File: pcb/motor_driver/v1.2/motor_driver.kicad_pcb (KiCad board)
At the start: 4 copper layers, 50 x 50 mm, 93 parts, among them J1 XT60PW-M, J2 1-84953-1, J3 Conn_ARM_JTAG_SWD_10, J5 Conn, Q1 BSS138, Q2 HP8K22TB, Q3 HP8K22TB, Q4 HP8K22TB, SW1 RESET, SW2 USER, U1 USBLC6-4SC6, U10 STM32G431CB, U12 MCP2562-E-SN, U3 DRV8323S, U4 a1333, U8 ADP151AUJZ-3.3-R7, U9 NJM12877F33-TE1, Y1 XRCGB16M000FXN02R0

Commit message: perf: fix pcb for v1.2
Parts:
- removed the C22 at (123.7, 100.7)
- removed the C23 at (125.7, 116.1)
- removed the C28 at (133.1, 104.3)
- removed C29: 0.1u, Capacitor_SMD:C_0603_1608Metric
- removed the C5 at (103.6, 78.9)
- removed the D1 at (100.5, 120.2)
- removed the D2 at (103.4, 120.2)
- removed the D3 at (106.3, 120.2)
- removed the Q1 at (136.1, 115.0)
- removed the R1 at (100.5, 123.2)
- removed the R2 at (103.4, 123.2)
- removed the R20 at (136.1, 112.1)
- removed the R21 at (110.5, 116.9)
- removed the R3 at (106.3, 123.2)
- removed SP1: SMT-0440, omni:STM0440-T-R
- removed the U1 at (106.5, 78.6)
- added C6: 1u, Capacitor_SMD:C_0603_1608Metric_Pad1.08x0.95mm_HandSolder, F.Cu at (103.5, 112.0)
- C1, C2, C3, C4, C9: footprint Capacitor_SMD:C_0603_1608Metric -> Capacitor_SMD:C_0603_1608Metric_Pad1.08x0.95mm_HandSolder
- C13: renamed from C14; footprint Capacitor_SMD:C_0603_1608Metric -> Capacitor_SMD:C_0603_1608Metric_Pad1.08x0.95mm_HandSolder
- C14: renamed from C15; footprint Capacitor_SMD:C_0603_1608Metric -> Capacitor_SMD:C_0603_1608Metric_Pad1.08x0.95mm_HandSolder
- C15: renamed from C16; footprint Capacitor_SMD:C_0603_1608Metric -> Capacitor_SMD:C_0603_1608Metric_Pad1.08x0.95mm_HandSolder
- C16: renamed from C17; footprint Capacitor_SMD:C_0603_1608Metric -> Capacitor_SMD:C_0603_1608Metric_Pad1.08x0.95mm_HandSolder
- C17: renamed from C18; footprint Capacitor_SMD:C_0603_1608Metric -> Capacitor_SMD:C_0603_1608Metric_Pad1.08x0.95mm_HandSolder
- C18: renamed from C19; footprint Capacitor_SMD:C_0603_1608Metric -> Capacitor_SMD:C_0603_1608Metric_Pad1.08x0.95mm_HandSolder
- C21: renamed from C25; footprint Capacitor_SMD:C_0603_1608Metric -> Capacitor_SMD:C_0603_1608Metric_Pad1.08x0.95mm_HandSolder
- C24: value 2.2u -> 0.1u
- C26: renamed from C33; footprint Capacitor_SMD:C_0603_1608Metric -> Capacitor_SMD:C_0603_1608Metric_Pad1.08x0.95mm_HandSolder
- C5: renamed from C7; footprint Capacitor_SMD:C_0402_1005Metric -> Capacitor_SMD:C_0603_1608Metric_Pad1.08x0.95mm_HandSolder
- D1: renamed from D4; footprint LED_SMD:LED_0402_1005Metric -> LED_SMD:LED_0603_1608Metric
- D2: renamed from D5; footprint LED_SMD:LED_0402_1005Metric -> LED_SMD:LED_0603_1608Metric
- D3: renamed from D6; footprint LED_SMD:LED_0402_1005Metric -> LED_SMD:LED_0603_1608Metric
- D4: renamed from D7; footprint LED_SMD:LED_0402_1005Metric -> LED_SMD:LED_0603_1608Metric
- D5: renamed from D8; footprint LED_SMD:LED_0402_1005Metric -> LED_SMD:LED_0603_1608Metric
- D6: renamed from D9; footprint LED_SMD:LED_0402_1005Metric -> LED_SMD:LED_0603_1608Metric
- D7: renamed from D10; footprint LED_SMD:LED_0402_1005Metric -> LED_SMD:LED_0603_1608Metric
- J1: value XT60PW-M -> XT30
- R17: renamed from R22; footprint Resistor_SMD:R_0603_1608Metric -> Resistor_SMD:R_0603_1608Metric_Pad0.98x0.95mm_HandSolder
- R18: renamed from R24; footprint Resistor_SMD:R_0603_1608Metric -> Resistor_SMD:R_0603_1608Metric_Pad0.98x0.95mm_HandSolder
- R19: renamed from R23; footprint Resistor_SMD:R_0603_1608Metric -> Resistor_SMD:R_0603_1608Metric_Pad0.98x0.95mm_HandSolder
- R20: renamed from R25; footprint Resistor_SMD:R_0603_1608Metric -> Resistor_SMD:R_0603_1608Metric_Pad0.98x0.95mm_HandSolder
- SW1, SW2: footprint bldc_lib:SKRPACE010 -> half_mouse_lib:TVAF06-A020B-R
- moved C21 1.86 mm to (109.5, 116.5), turned to 90 degrees
- moved C24 1.55 mm to (131.7, 112.5)
- moved R18 0.81 mm to (115.4, 116.5)
- moved D7 0.70 mm to (133.6, 88.3)
- moved D6 0.68 mm to (135.4, 88.3)
- moved D2 0.60 mm to (118.8, 122.8)
- moved R11 0.60 mm to (118.8, 119.8)
- moved D3 0.59 mm to (121.6, 122.8)
- moved R13 0.59 mm to (121.6, 119.8)
- moved R10 0.57 mm to (130.1, 119.8)
- moved D1 0.57 mm to (130.1, 122.9)
- moved D4 0.56 mm to (124.4, 122.8)
- moved R14 0.56 mm to (124.4, 119.8)
- moved D5 0.55 mm to (127.2, 122.8)
- moved R15 0.55 mm to (127.2, 119.8)
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- renumbered C11 to C10, C12 to C11, C13 to C12, C20 to C19, C21 to C20, C26 to C22, C27 to C23, C30 to C25, C34 to C27, C36 to C28, C10 to C7, J2 to J3, J3 to J4, Q2 to Q1, Q3 to Q2, Q4 to Q3, R4 to R1, R13 to R10, R14 to R11, R15 to R12, R16 to R13, R17 to R14, R18 to R15, R19 to R16, R5 to R2, R26 to R21, R27 to R22, R28 to R23, R6 to R3, R7 to R4, R8 to R5, R9 to R6, R10 to R7, R11 to R8, R12 to R9, U3 to U1, U4 to U2, U8 to U3, U9 to U4, U10 to U5, U12 to U6
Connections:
- net /drv8323/INHA renamed /stm32g431cb/TIM4_INHA
- net /drv8323/INHB renamed /stm32g431cb/TIM4_INHB
- net /drv8323/INHC renamed /stm32g431cb/TIM4_INHC
- C24 pad 1: Net-(C24-Pad1) -> +3.3V
- C26 pad 1: +3.3V -> /stm32g431cb/SW1
- R18 pad 2: Net-(R24-Pad2) -> /stm32g431cb/SW1
- SW1 pad 1: Net-(R21-Pad2) -> /stm32g431cb/NRST
- SW1 pad 2: unconnected-(SW1-Pad2) -> GND
- SW2 pad 1: Net-(R24-Pad2) -> GND
- U1 pad 33: +3.3V -> Net-(U1-DVDD)
- U5 pad 19: Net-(C23-Pad1) -> GND
- U5 pad 23: Net-(C24-Pad1) -> GND
- U5 pad 35: Net-(C28-Pad1) -> GND
- U5 pad 47: Net-(C22-Pad1) -> GND
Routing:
- net /stm32g431cb/TIM4_INHA: track 52.7 -> 40.1 mm
- net /stm32g431cb/TIM4_INHB: track 47.0 -> 37.0 mm
- net Net-(Q1-Pad3): track 8.27 -> 0.00 mm
- net /stm32g431cb/TIM15_SP: track 8.17 -> 0.00 mm, vias 1 -> 0
- net /stm32g431cb/TIM4_INHC: track 42.5 -> 34.8 mm
- net /drv8323/HALL_W: track 48.2 -> 40.7 mm
- net /drv8323/HALL_U: track 47.8 -> 40.7 mm, vias 3 -> 2
- net GND: track 871.3 -> 864.7 mm, vias 105 -> 107
- net +3.3V: track 44.9 -> 39.2 mm, vias 8 -> 7
- net /drv8323/HALL_V: track 45.1 -> 40.5 mm
- net Net-(C23-Pad1): track 3.90 -> 0.00 mm
- net Net-(C24-Pad1): track 3.19 -> 0.00 mm
- net +5V: track 35.4 -> 32.4 mm, vias 6 -> 5
- net Net-(U1-DVDD): track 0.00 -> 2.56 mm
- net Net-(C22-Pad1): track 2.50 -> 0.00 mm
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
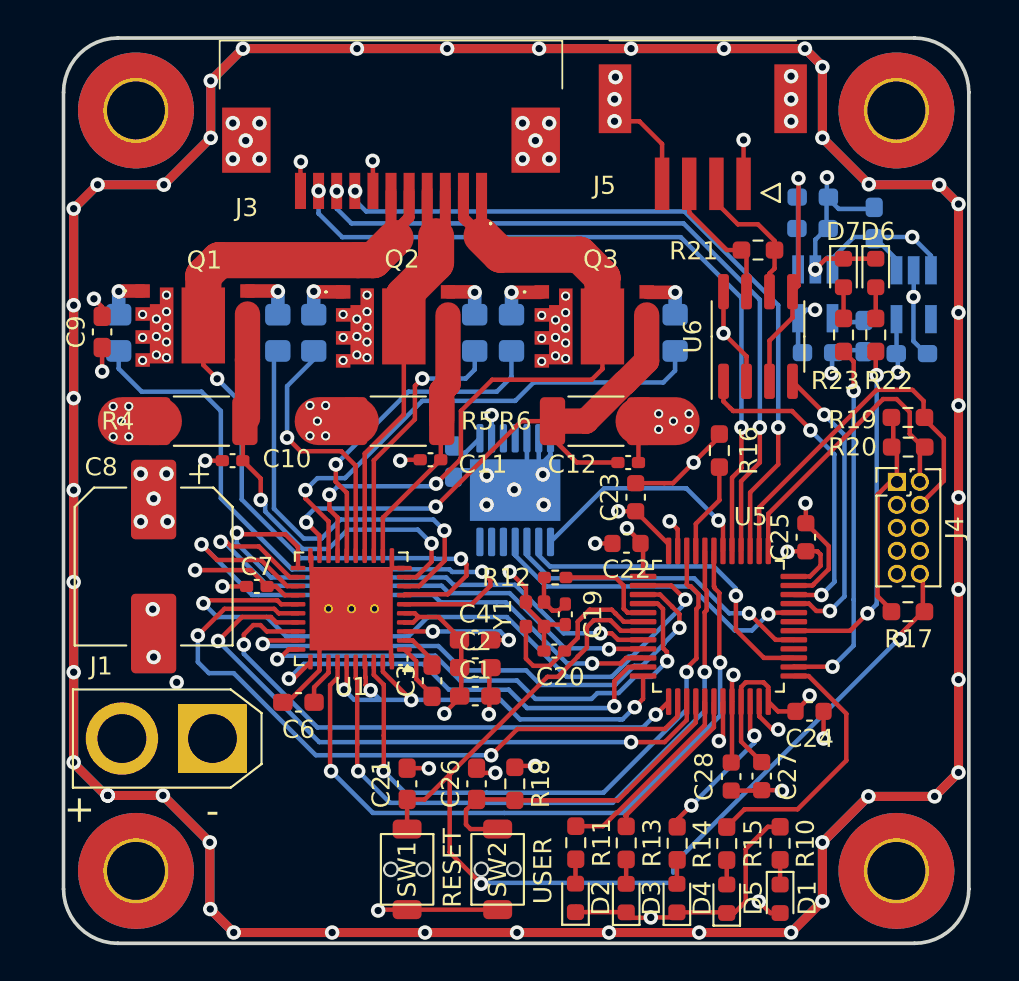
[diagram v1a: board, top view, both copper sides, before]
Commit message: perf: update motor driver pdb
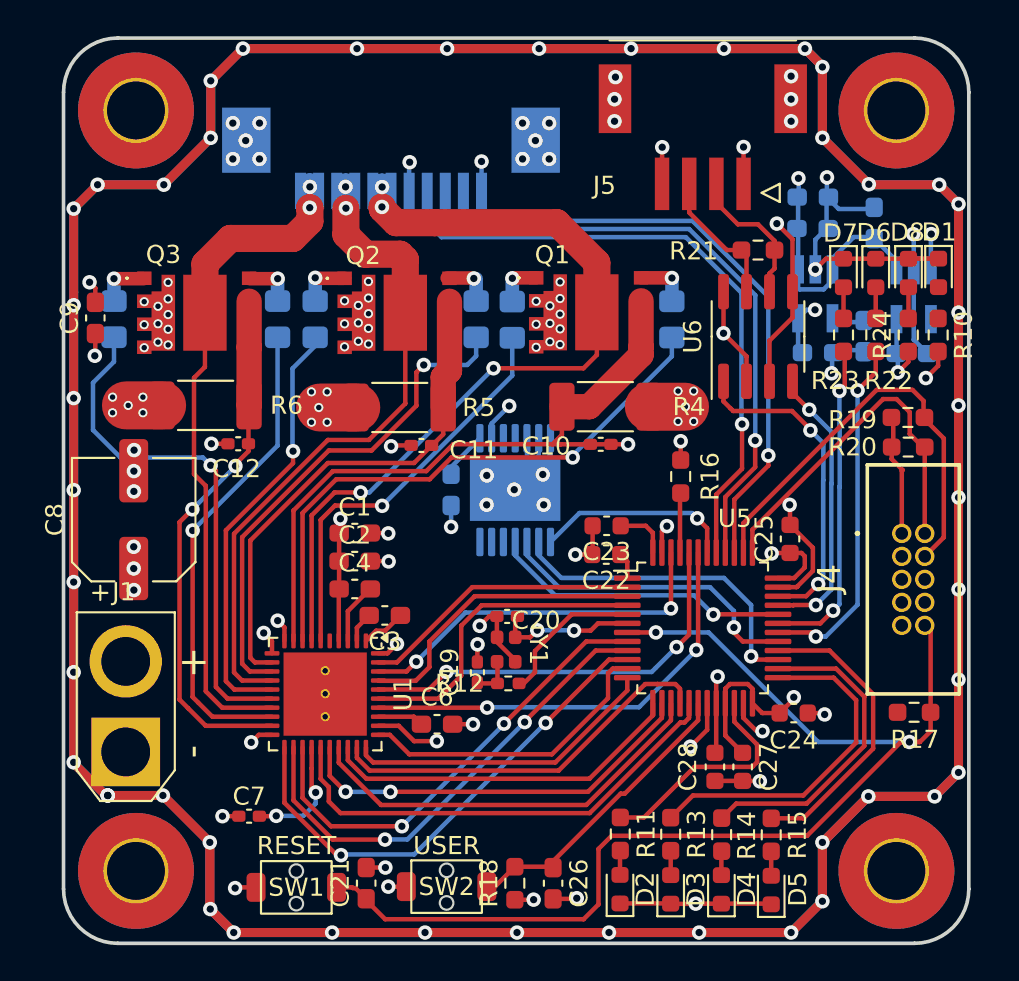
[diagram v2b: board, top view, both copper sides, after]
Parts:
- added D8: LED, LED_SMD:LED_0603_1608Metric, F.Cu at (137.2, 88.3)
- added R24: 1k, Resistor_SMD:R_0603_1608Metric_Pad0.98x0.95mm_HandSolder, F.Cu at (137.2, 91.7)
- C8: footprint Capacitor_SMD:CP_Elec_8x10.5 -> Capacitor_SMD:CP_Elec_6.3x3.9
- J3: moved to B.Cu
- J4: footprint Connector_PinHeader_1.27mm:PinHeader_2x05_P1.27mm_Vertical -> mylib:322110010000
- moved D1 35.7 mm to (138.8, 88.3)
- moved R10 29.4 mm to (138.8, 91.7)
- moved R4 22.3 mm to (120.5, 95.7), turned to 180 degrees
- moved Q3 22.0 mm to (97.9, 90.5)
- moved R3 22.0 mm to (93.3, 90.8)
- moved R9 22.0 mm to (102.3, 90.8)
- moved R7 21.8 mm to (124.1, 90.9)
- moved Q1 21.7 mm to (119.5, 90.5)
- moved R1 21.7 mm to (115.3, 90.9)
- moved R6 21.6 mm to (98.4, 95.6), turned to 0 degrees
- moved C12 21.6 mm to (100.2, 97.7), turned to 180 degrees
- moved C10 20.4 mm to (120.2, 97.8), turned to 0 degrees
- moved C7 12.7 mm to (100.8, 118.3)
- moved C1 11.2 mm to (106.6, 102.7)
- moved C2 8.89 mm to (106.6, 104.2)
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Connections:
- D1 pad 1: Net-(D1-K) -> GND
- D1 pad 2: +3.3V -> Net-(D1-A)
- R10 pad 1: Net-(D1-K) -> +3.3V
- R10 pad 2: GND -> Net-(D1-A)
- U1 pad 21: /stm32g431cb/ADC1_1 -> /stm32g431cb/ADC1_3
- U1 pad 23: /stm32g431cb/ADC1_3 -> /stm32g431cb/ADC1_1
- U1 pad 35: /stm32g431cb/INLX -> /stm32g431cb/INLA
- U1 pad 37: /stm32g431cb/INLX -> /stm32g431cb/INLB
- U1 pad 39: /stm32g431cb/INLX -> /stm32g431cb/INLC
- U5 pad 12: /stm32g431cb/INLX -> /stm32g431cb/DRV_ENABLE
- U5 pad 16: /stm32g431cb/SW1 -> /stm32g431cb/SS_DRV
- U5 pad 17: /stm32g431cb/LED1 -> /stm32g431cb/FAULTB
- U5 pad 18: /stm32g431cb/LED2 -> /stm32g431cb/SW1
- U5 pad 2: /stm32g431cb/FAULTB -> /stm32g431cb/INLC
- U5 pad 22: /stm32g431cb/LED3 -> /stm32g431cb/LED1
- U5 pad 25: /stm32g431cb/LED4 -> /stm32g431cb/LED2
- U5 pad 26: /stm32g431cb/LED_CAN_RX -> /stm32g431cb/LED3
- U5 pad 28: /stm32g431cb/TIM15_SP -> /stm32g431cb/LED4
- U5 pad 3: /stm32g431cb/SS_DRV -> /stm32g431cb/INLB
- U5 pad 31: unconnected-(U5-PA9-Pad31) -> /stm32g431cb/LED_CAN_RX
- U5 pad 39: /drv8323/HALL_V -> /drv8323/HALL_W
- U5 pad 4: /stm32g431cb/DRV_ENABLE -> /stm32g431cb/INLA
- U5 pad 41: /drv8323/HALL_W -> /drv8323/HALL_V
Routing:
- net GND: track 864.7 -> 837.6 mm, vias 107 -> 120
- net /stm32g431cb/INLX: track 25.7 -> 0.00 mm, vias 4 -> 0
- net /stm32g431cb/INLA: track 0.00 -> 17.5 mm
- net /stm32g431cb/INLB: track 0.00 -> 16.5 mm
- net /stm32g431cb/TIM4_INHA: track 40.1 -> 24.3 mm
- net /stm32g431cb/INLC: track 0.00 -> 15.5 mm
- net /drv8323/SPI1_MISO: track 38.0 -> 22.8 mm
- net /stm32g431cb/TIM4_INHC: track 34.8 -> 20.7 mm
- net /stm32g431cb/TIM4_INHB: track 37.0 -> 22.9 mm
- net /drv8323/SLB: track 14.8 -> 28.4 mm
- net /drv8323/SLA: track 26.0 -> 39.2 mm, vias 2 -> 0
- net /stm32g431cb/FAULTB: track 39.3 -> 26.3 mm, vias 2 -> 0
- net /drv8323/GLB: track 15.0 -> 28.0 mm
- net /drv8323/SHB: track 24.7 -> 36.8 mm, vias 0 -> 2
- net /drv8323/GHA: track 34.7 -> 22.7 mm
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
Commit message: wip: can settings
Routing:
- net +3.3V: track 31.1 -> 32.0 mm, vias 5 -> 7
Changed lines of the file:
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@@
-	)
-	(segment
-		(start 121.66 104.225)
-		(end 121.275 103.84)
-		(width 0.25)
-		(layer "F.Cu")
-		(net 8)
 	)
 	(segment
@@
 	)
 	(segment
+		(start 121.315 102.27)
+		(end 121.295 102.25)
+		(width 0.25)
+		(layer "F.Cu")
+		(net 8)
+	)
+	(segment
 		(start 136.3504 96.2814)
 		(end 136.335 96.266)
@@
 	)
 	(segment
+		(start 123.0725 102.8425)
+		(end 122.5 102.27)
+		(width 0.25)
+		(layer "F.Cu")
+		(net 8)
+	)
+	(segment
+		(start 122.03 103.84)
+		(end 121.275 103.84)
+		(width 0.25)
+		(layer "F.Cu")
+		(net 8)
+	)
+	(segment
 		(start 136.82 99.22)
 		(end 136.82 102.67)
@@
 	)
 	(segment
-		(start 121.66 105.14)
-		(end 121.66 104.225)
+		(start 122.3 104.28)
+		(end 122.3 104.09)
 		(width 0.25)
 		(layer "F.Cu")
@@
 	)
 	(segment
-		(start 122.68 102.25)
-		(end 121.295 102.25)
+		(start 122.04 103.83)
+		(end 122.03 103.84)
 		(width 0.25)
 		(layer "F.Cu")
@@
 	)
 	(segment
-		(start 123.0725 102.6425)
-		(end 122.68 102.25)
-		(width 0.25)
-		(layer "F.Cu")
-		(net 8)
-	)
-	(segment
 		(start 128.5725 111.249315)
 		(end 128.311985 110.9888)
@@
 	)
 	(segment
+		(start 121.66 104.92)
+		(end 122.3 104.28)
+		(width 0.25)
+		(layer "F.Cu")
+		(net 8)
+	)
+	(segment
+		(start 122.3 104.09)
+		(end 122.04 103.83)
+		(width 0.25)
+		(layer "F.Cu")
+		(net 8)
+	)
+	(segment
 		(start 129.6573 103.7504)
 		(end 129.6325 103.7752)
@@
 	)
 	(segment
-		(start 123.0725 103.7275)
-		(end 123.0725 102.6425)
-		(width 0.25)
-		(layer "F.Cu")
-		(net 8)
-	)
-	(segment
 		(start 129.1124 112.5924)
 		(end 130.0773 112.5924)
@@
 	)
 	(segment
+		(start 121.66 105.14)
+		(end 121.66 104.92)
+		(width 0.25)
+		(layer "F.Cu")
+		(net 8)
+	)
+	(segment
 		(start 136.87 99.17)
 		(end 136.82 99.22)
@@
 	)
 	(segment
+		(start 122.5 102.27)
+		(end 121.315 102.27)
+		(width 0.25)
+		(layer "F.Cu")
+		(net 8)
+	)
+	(segment
 		(start 131.4613 103.9276)
 		(end 131.2841 103.7504)
@@
 	)
 	(segment
+		(start 123.0725 103.7275)
+		(end 123.0725 102.8425)
+		(width 0.25)
+		(layer "F.Cu")
+		(net 8)
+	)
+	(segment
 		(start 116.480391 122.905)
 		(end 116.4875 122.897891)
@@
 	)
 	(via
+		(at 122.5 102.27)
+		(size 0.8)
+		(drill 0.4)
+		(layers "F.Cu" "B.Cu")
+		(net 8)
+	)
+	(via
 		(at 116.4875 122.897891)
 		(size 0.8)
@@
 		(size 0.8)
 		(drill 0.4)
+		(layers "F.Cu" "B.Cu")
+		(net 8)
+	)
+	(via
+		(at 122.3 104.28)
+		(size 0.8)
+		(drill 0.4)

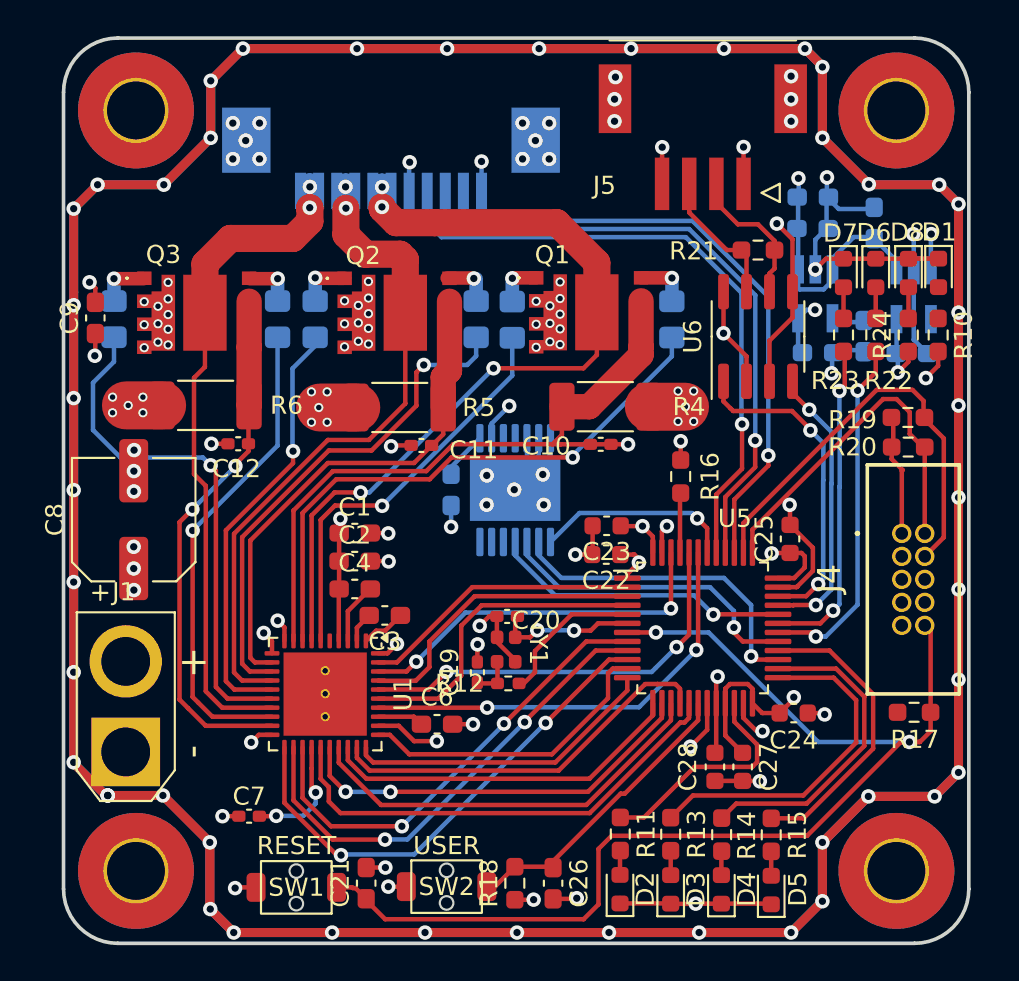
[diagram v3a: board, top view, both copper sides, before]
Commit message: feat: add additional CAN connetctor
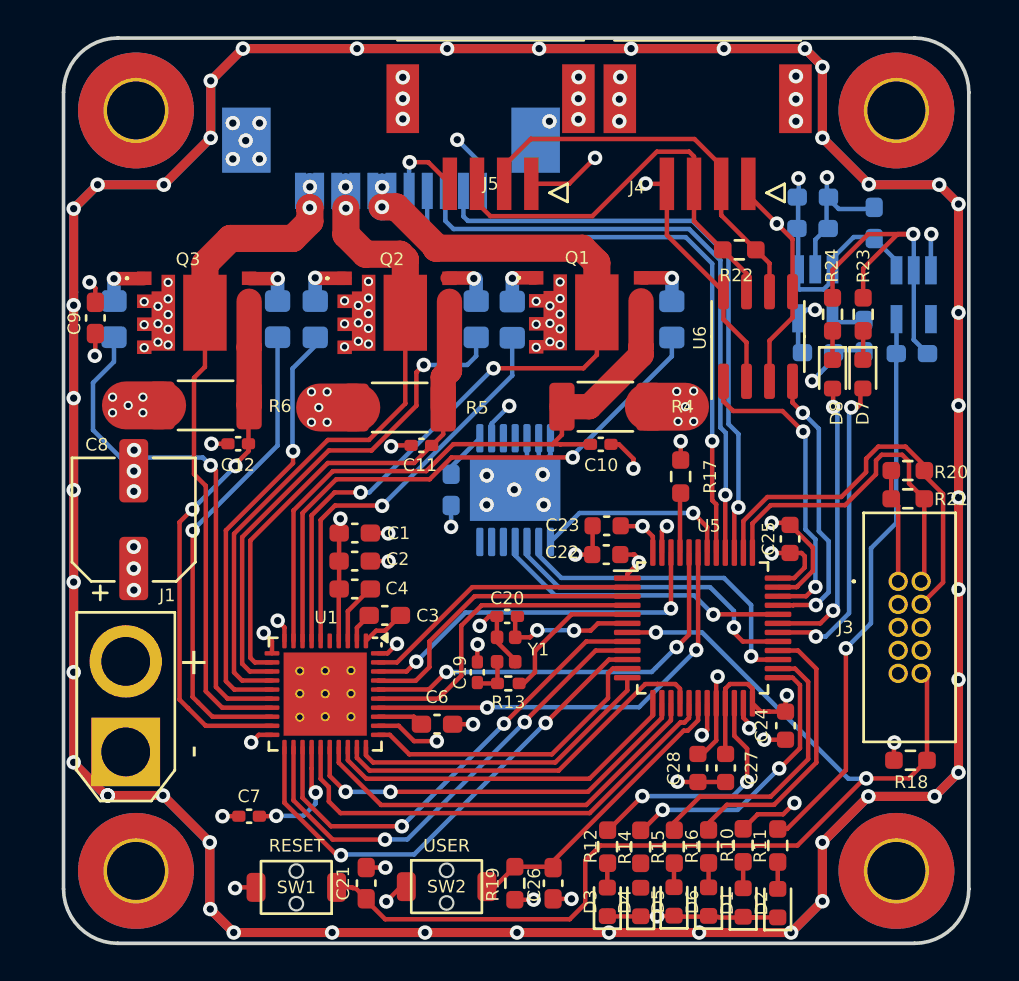
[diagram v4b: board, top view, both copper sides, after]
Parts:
- removed the D8 at (137.2, 88.3)
- removed the R24 at (137.2, 91.7)
- added D2: LED, LED_SMD:LED_0603_1608Metric, F.Cu at (130.0, 123.1)
- added J5: Conn, mylib:21322604YY, F.Cu at (114.1, 83.4)
- added R11: 1k, Resistor_SMD:R_0603_1608Metric_Pad0.98x0.95mm_HandSolder, F.Cu at (130.0, 119.9)
- J4: renamed from J5; footprint bldc_lib:21322604YY -> mylib:21322604YY
- moved D1 36.4 mm to (128.1, 123.1), turned to 90 degrees
- moved R10 30.2 mm to (128.1, 119.9), turned to -90 degrees
- moved D7 5.64 mm to (134.7, 93.9)
- moved D8 5.63 mm to (133.0, 93.9)
- moved D6 3.52 mm to (126.2, 123.0)
- moved R16 3.52 mm to (126.2, 120.0)
- moved R20 2.93 mm to (137.2, 99.2)
- moved R21 2.86 mm to (137.2, 100.8)
- moved D5 2.70 mm to (124.2, 123.0)
- moved R15 2.70 mm to (124.3, 120.0)
- moved R18 2.66 mm to (137.3, 115.2)
- moved J3 2.66 mm to (136.6, 105.3)
- moved D4 1.80 mm to (122.4, 123.0)
- moved R14 1.80 mm to (122.4, 120.0)
- moved R23 1.33 mm to (134.7, 90.6)
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- renumbered D2 to D3, D3 to D4, D4 to D5, D5 to D6, D6 to D7, D7 to D8, J3 to J2, J4 to J3, R11 to R12, R12 to R13, R13 to R14, R14 to R15, R15 to R16, R16 to R17, R17 to R18, R18 to R19, R19 to R20, R20 to R21, R21 to R22, R22 to R23, R23 to R24
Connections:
- D7 pad 1: GND -> Net-(D7-K)
- D7 pad 2: Net-(D6-A) (its old number) -> /stm32g431cb/LED_CAN_TX
- D8 pad 1: GND -> Net-(D8-K)
- D8 pad 2: Net-(D7-A) -> /stm32g431cb/LED_CAN_RX
- R23 pad 1: /stm32g431cb/LED_CAN_TX -> Net-(D7-K)
- R23 pad 2: Net-(D6-A) (its old number) -> GND
- R24 pad 1: /stm32g431cb/LED_CAN_RX -> Net-(D8-K)
- R24 pad 2: Net-(D7-A) -> GND
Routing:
- net GND: track 837.6 -> 854.7 mm
- net /stm32g431cb/CAN_H: track 7.75 -> 23.6 mm
- net /stm32g431cb/CAN_L: track 8.05 -> 22.3 mm
- net +3.3VA: track 64.2 -> 75.3 mm
- net +5V: track 33.2 -> 39.8 mm
- net /stm32g431cb/NRST: track 64.6 -> 60.1 mm
- net /stm32g431cb/LED2: track 19.1 -> 15.4 mm, vias 0 -> 2
- net /stm32g431cb/LED_CAN_TX: track 19.6 -> 17.5 mm
- net /stm32g431cb/LED_CAN_RX: track 17.9 -> 15.8 mm
- net /stm32g431cb/LED3: track 17.7 -> 15.5 mm
- net /drv8323/SLA: track 39.2 -> 37.1 mm
- net Net-(D8-A): track 1.73 -> 0.00 mm
- net Net-(D7-A): track 1.72 -> 0.00 mm
- net Net-(D6-A) (its old number): track 1.72 -> 0.00 mm
- net +3.3V: track 32.0 -> 33.6 mm, vias 7 -> 8
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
